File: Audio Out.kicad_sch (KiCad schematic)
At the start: 20 parts

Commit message: some cleanup
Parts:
- U9: MnfNumber (none) -> OPA1688IDR
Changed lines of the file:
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@@
+      (effects (font (size 1.27 1.27)) hide)
+    )
+    (property "MnfNumber" "OPA1688IDR" (at 128.27 53.34 0)
       (effects (font (size 1.27 1.27)) hide)
     )
@@
       (effects (font (size 1.27 1.27)) hide)
     )
+    (property "MnfNumber" "OPA1688IDR" (at 130.81 133.35 0)
+      (effects (font (size 1.27 1.27)) hide)
+    )
     (pin "1")
     (pin "2")
@@
       (effects (font (size 1.27 1.27)) hide)
     )
+    (property "MnfNumber" "OPA1688IDR" (at 54.61 97.79 0)
+      (effects (font (size 1.27 1.27)) hide)
+    )

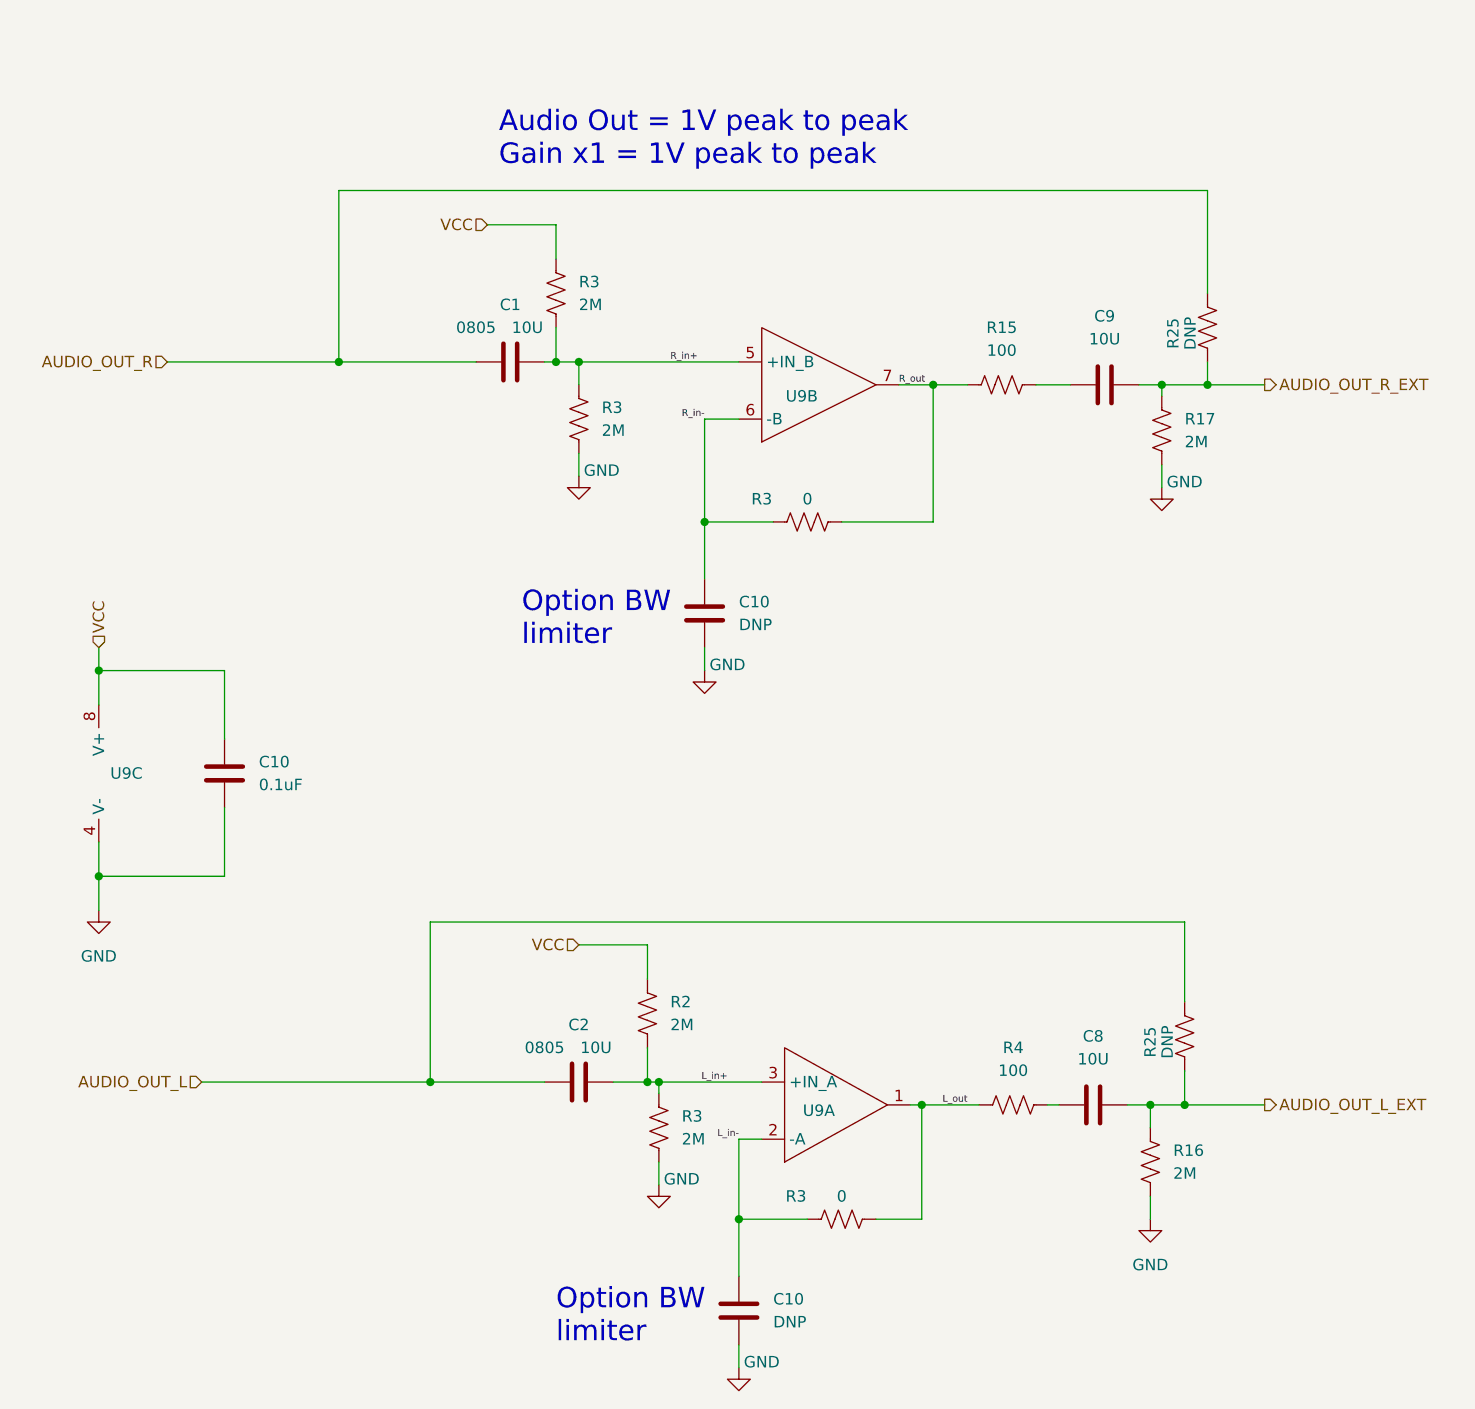
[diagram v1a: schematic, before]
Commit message: updated parts with those available on jlpcb
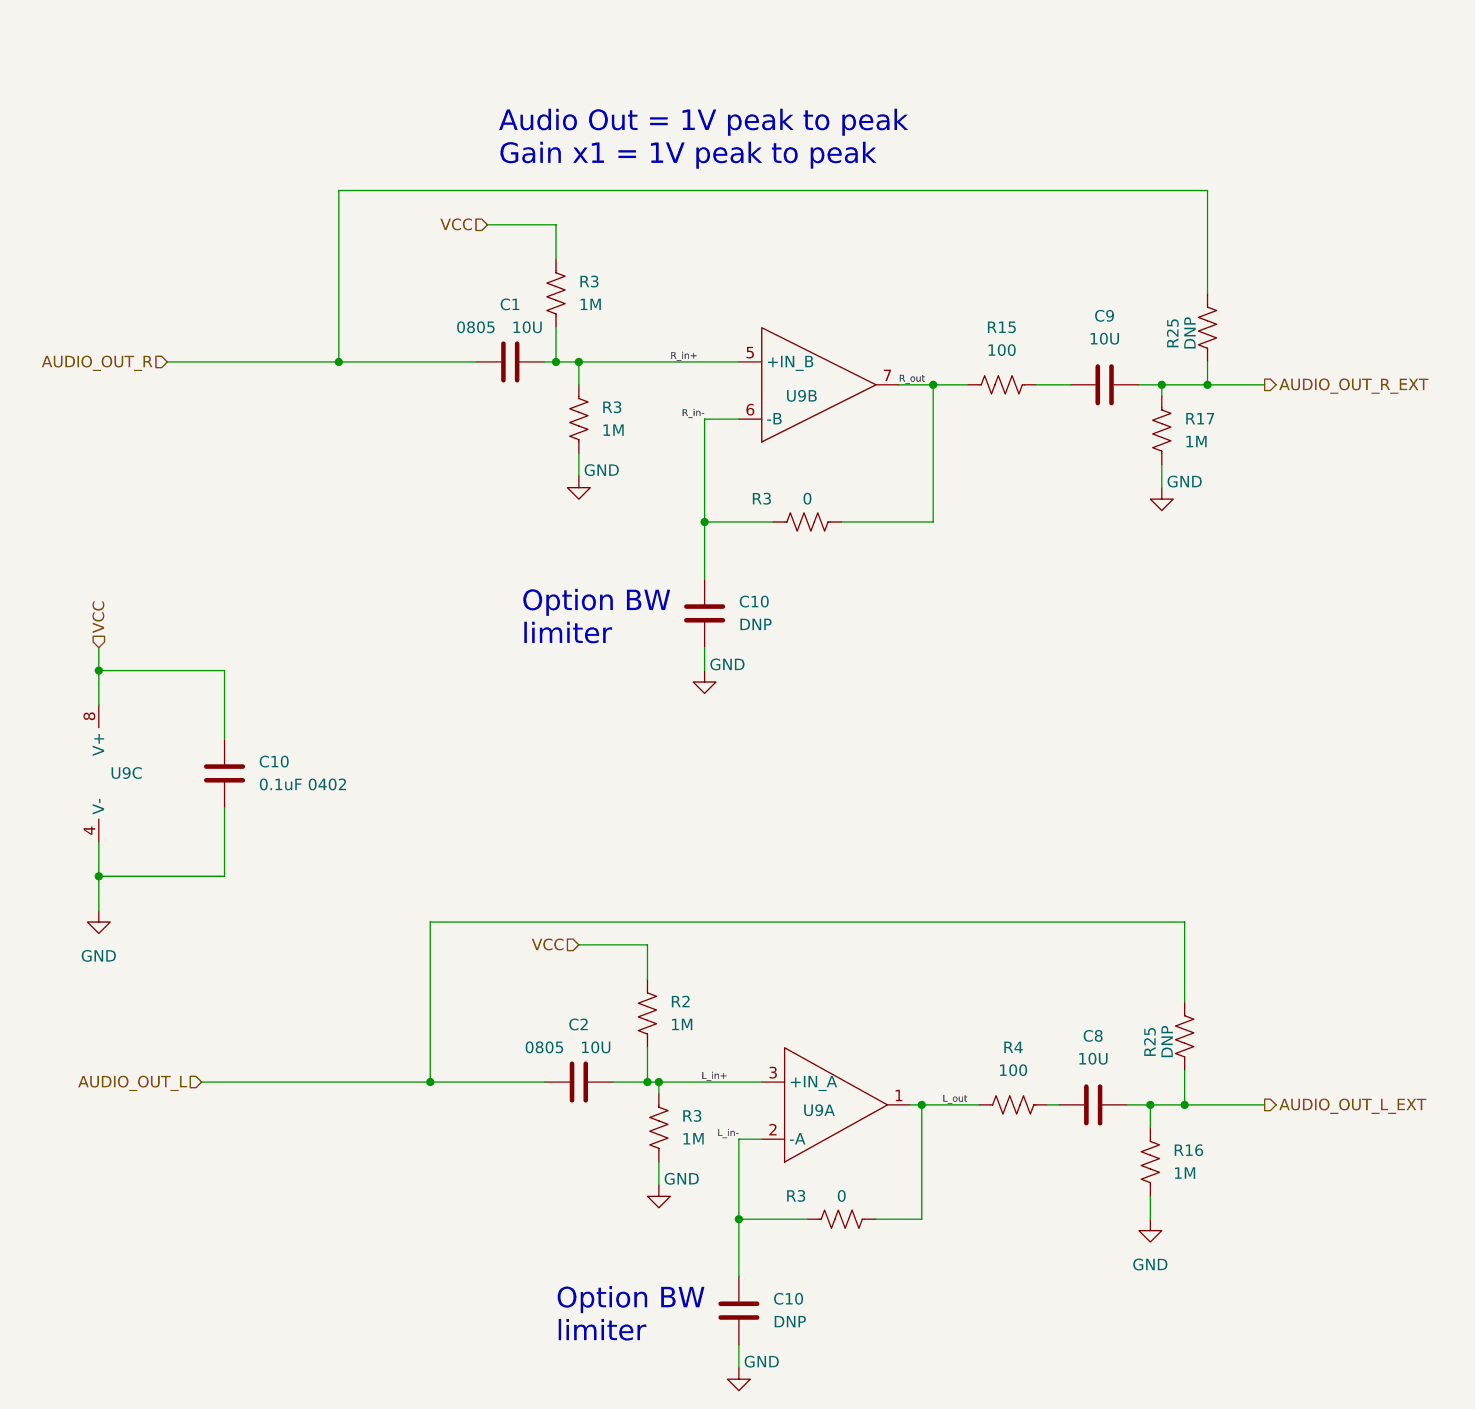
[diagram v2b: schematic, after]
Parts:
- C10: value 0.1uF -> 0.1uF 0402
- R16, R17, R2, R3: value 2M -> 1M
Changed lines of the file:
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@@
       (effects (font (size 1.27 1.27)) (justify left))
     )
-    (property "Value" "2M" (at 110.49 58.42 0)
+    (property "Value" "1M" (at 110.49 58.42 0)
       (effects (font (size 1.27 1.27)) (justify left))
     )
@@
       (effects (font (size 1.27 1.27)) (justify left))
     )
-    (property "Value" "2M" (at 107.95 44.45 0)
+    (property "Value" "1M" (at 107.95 44.45 0)
       (effects (font (size 1.27 1.27)) (justify left))
     )
@@
       (effects (font (size 1.27 1.27)) (justify left))
     )
-    (property "Value" "2M" (at 118.11 124.46 0)
+    (property "Value" "1M" (at 118.11 124.46 0)
       (effects (font (size 1.27 1.27)) (justify left))
     )
@@
       (effects (font (size 1.27 1.27)) (justify left))
     )
-    (property "Value" "2M" (at 119.38 137.16 0)
+    (property "Value" "1M" (at 119.38 137.16 0)
       (effects (font (size 1.27 1.27)) (justify left))
     )
@@
       (effects (font (size 1.27 1.27)) (justify left))
     )
-    (property "Value" "2M" (at 173.99 140.97 0)
+    (property "Value" "1M" (at 173.99 140.97 0)
       (effects (font (size 1.27 1.27)) (justify left))
     )
@@
       (effects (font (size 1.27 1.27)) (justify left))
     )
-    (property "Value" "2M" (at 175.26 59.69 0)
+    (property "Value" "1M" (at 175.26 59.69 0)
       (effects (font (size 1.27 1.27)) (justify left))
     )
@@
       (effects (font (size 1.27 1.27)) (justify left))
     )
-    (property "Value" "0.1uF" (at 72.39 97.79 0)
-      (effects (font (size 1.27 1.27)) (justify left))
-    )
+    (property "Value" "0.1uF 0402" (at 72.39 97.79 0)
+      (effects (font (size 1.27 1.27)) (justify left))
+    )

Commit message: Moved everything to the top side
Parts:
- C10: footprint Capacitor_SMD:C_0402_1005Metric -> Capacitor_SMD:C_0603_1608Metric
- R15, R16, R17, R2, R25, R3, R4: footprint Resistor_SMD:R_0402_1005Metric -> Resistor_SMD:R_0603_1608Metric
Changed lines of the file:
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@@
       (effects (font (size 1.27 1.27)) (justify left))
     )
-    (property "Footprint" "Resistor_SMD:R_0402_1005Metric" (at 108.966 57.404 90)
+    (property "Footprint" "Resistor_SMD:R_0603_1608Metric" (at 108.966 57.404 90)
       (effects (font (size 1.27 1.27)) hide)
     )
@@
       (effects (font (size 1.27 1.27)))
     )
-    (property "Footprint" "Resistor_SMD:R_0402_1005Metric" (at 137.414 145.034 90)
+    (property "Footprint" "Resistor_SMD:R_0603_1608Metric" (at 137.414 145.034 90)
       (effects (font (size 1.27 1.27)) hide)
     )
@@
       (effects (font (size 1.27 1.27)) (justify left))
     )
-    (property "Footprint" "Resistor_SMD:R_0402_1005Metric" (at 106.426 43.434 90)
+    (property "Footprint" "Resistor_SMD:R_0603_1608Metric" (at 106.426 43.434 90)
       (effects (font (size 1.27 1.27)) hide)
     )
@@
       (effects (font (size 1.27 1.27)) (justify left))
     )
-    (property "Footprint" "Resistor_SMD:R_0402_1005Metric" (at 116.586 123.444 90)
+    (property "Footprint" "Resistor_SMD:R_0603_1608Metric" (at 116.586 123.444 90)
       (effects (font (size 1.27 1.27)) hide)
     )
@@
       (effects (font (size 1.27 1.27)))
     )
-    (property "Footprint" "Resistor_SMD:R_0402_1005Metric" (at 133.604 67.564 90)
+    (property "Footprint" "Resistor_SMD:R_0603_1608Metric" (at 133.604 67.564 90)
       (effects (font (size 1.27 1.27)) hide)
     )
@@
       (effects (font (size 1.27 1.27)) (justify left))
     )
-    (property "Footprint" "Capacitor_SMD:C_0402_1005Metric" (at 122.8852 82.55 0)
+    (property "Footprint" "Capacitor_SMD:C_0603_1608Metric" (at 122.8852 82.55 0)
       (effects (font (size 1.27 1.27)) hide)
     )
@@
       (effects (font (size 1.27 1.27)) (justify left))
     )
-    (property "Footprint" "Resistor_SMD:R_0402_1005Metric" (at 117.856 136.144 90)
+    (property "Footprint" "Resistor_SMD:R_0603_1608Metric" (at 117.856 136.144 90)
       (effects (font (size 1.27 1.27)) hide)
     )
@@
       (effects (font (size 1.27 1.27)) (justify left))
     )
-    (property "Footprint" "Resistor_SMD:R_0402_1005Metric" (at 172.466 139.954 90)
+    (property "Footprint" "Resistor_SMD:R_0603_1608Metric" (at 172.466 139.954 90)
       (effects (font (size 1.27 1.27)) hide)
     )
@@
       (effects (font (size 1.27 1.27)) (justify left))
     )
-    (property "Footprint" "Resistor_SMD:R_0402_1005Metric" (at 173.736 58.674 90)
+    (property "Footprint" "Resistor_SMD:R_0603_1608Metric" (at 173.736 58.674 90)
       (effects (font (size 1.27 1.27)) hide)
     )
@@
       (effects (font (size 1.27 1.27)))
     )
-    (property "Footprint" "Resistor_SMD:R_0402_1005Metric" (at 174.244 125.476 90)
+    (property "Footprint" "Resistor_SMD:R_0603_1608Metric" (at 174.244 125.476 90)
       (effects (font (size 1.27 1.27)) hide)
     )
@@
       (effects (font (size 1.27 1.27)))
     )
-    (property "Footprint" "Resistor_SMD:R_0402_1005Metric" (at 156.464 132.334 90)
+    (property "Footprint" "Resistor_SMD:R_0603_1608Metric" (at 156.464 132.334 90)
       (effects (font (size 1.27 1.27)) hide)
     )
@@
       (effects (font (size 1.27 1.27)))
     )
-    (property "Footprint" "Resistor_SMD:R_0402_1005Metric" (at 176.784 46.736 90)
+    (property "Footprint" "Resistor_SMD:R_0603_1608Metric" (at 176.784 46.736 90)
       (effects (font (size 1.27 1.27)) hide)
     )
@@
       (effects (font (size 1.27 1.27)) (justify left))
     )
-    (property "Footprint" "Capacitor_SMD:C_0402_1005Metric" (at 69.5452 100.33 0)
+    (property "Footprint" "Capacitor_SMD:C_0603_1608Metric" (at 69.5452 100.33 0)
       (effects (font (size 1.27 1.27)) hide)
     )
@@
       (effects (font (size 1.27 1.27)))
     )
-    (property "Footprint" "Resistor_SMD:R_0402_1005Metric" (at 155.194 52.324 90)
+    (property "Footprint" "Resistor_SMD:R_0603_1608Metric" (at 155.194 52.324 90)
       (effects (font (size 1.27 1.27)) hide)
     )
@@
       (effects (font (size 1.27 1.27)) (justify left))
     )
-    (property "Footprint" "Capacitor_SMD:C_0402_1005Metric" (at 126.6952 160.02 0)
-      (effects (font (size 1.27 1.27)) hide)
-    )
+    (property "Footprint" "Capacitor_SMD:C_0603_1608Metric" (at 126.6952 160.02 0)
+      (effects (font (size 1.27 1.27)) hide)
+    )
